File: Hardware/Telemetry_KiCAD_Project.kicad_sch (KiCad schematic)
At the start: 3 parts, among them J1 TX SPI Debug, J2 RX SPI Debug, J3 Right Angle SMA Female

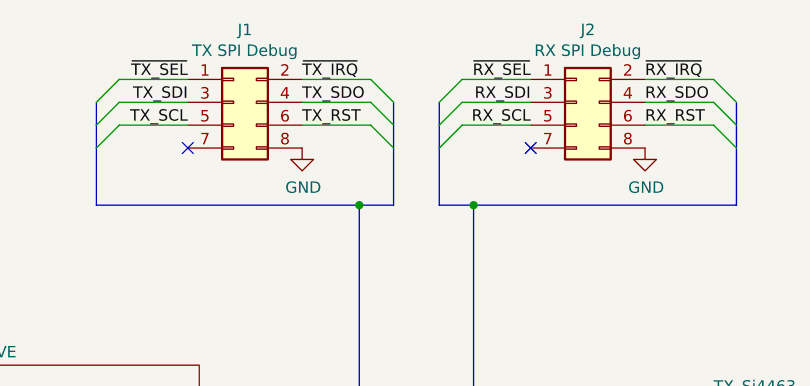
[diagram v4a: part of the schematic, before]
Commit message: Updated LCSC numbers, updated BOM file, added power LED.
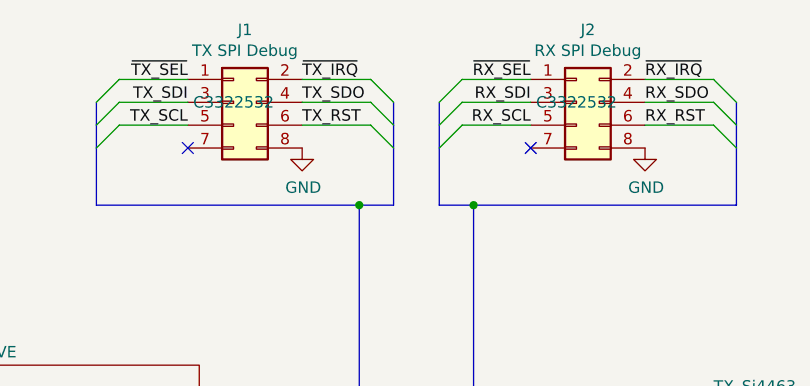
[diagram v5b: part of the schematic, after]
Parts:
- J1, J2: LCSC (none) -> C3322532
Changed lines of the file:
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@@
     (pin "1")
   )
-  (symbol (lib_id "Connector_Generic:Conn_02x04_Odd_Even") (at 107.95 24.13 0) (unit 1)
+  (symbol (lib_name "Conn_02x04_Odd_Even_1") (lib_id "Connector_Generic:Conn_02x04_Odd_Even") (at 107.95 24.13 0) (unit 1)
     (in_bom yes) (on_board yes)
     (property "Reference" "J1" (id 0) (at 109.22 16.0782 0))
@@
       (effects (font (size 1.27 1.27)) hide)
     )
+    (property "LCSC" "C3322532" (id 4) (at 107.95 24.13 0))
     (pin "1")
     (pin "2")
@@
       (effects (font (size 1.27 1.27)) hide)
     )
+    (property "LCSC" "C3322532" (id 4) (at 146.05 24.13 0))
     (pin "1")
     (pin "2")
@@
       (reference "#PWR047") (unit 1) (value "GND") (footprint "")
     )
+    (path "/00000000-0000-0000-0000-000061a107a5/7d5f7f73-c3ff-4d60-be90-7f89fb3f0e55"
+      (reference "#PWR048") (unit 1) (value "+3.3V") (footprint "")
+    )
+    (path "/00000000-0000-0000-0000-000061a107a5/32b6add9-6af3-4c4e-9640-6b64439e3a2a"
+      (reference "#PWR049") (unit 1) (value "GND") (footprint "")
+    )
     (path "/00000000-0000-0000-0000-000061a107a5/00000000-0000-0000-0000-000061a17dd9"
       (reference "#PWR050") (unit 1) (value "+3.3V") (footprint "")
@@
       (reference "D6") (unit 1) (value "Red") (footprint "LED_SMD:LED_0603_1608Metric_Pad1.05x0.95mm_HandSolder")
     )
+    (path "/00000000-0000-0000-0000-000061a107a5/8c687336-efb8-48b9-ac29-6b1477aa311d"
+      (reference "D7") (unit 1) (value "Red") (footprint "LED_SMD:LED_0603_1608Metric_Pad1.05x0.95mm_HandSolder")
+    )
     (path "/00000000-0000-0000-0000-000061a2ed84/00000000-0000-0000-0000-000061a399bc"
       (reference "FB1") (unit 1) (value "Ferrite_Bead_Small") (footprint "Capacitor_SMD:C_0603_1608Metric_Pad1.08x0.95mm_HandSolder")
@@
       (reference "R12") (unit 1) (value "4.7k") (footprint "Resistor_SMD:R_0603_1608Metric_Pad0.98x0.95mm_HandSolder")
     )
+    (path "/00000000-0000-0000-0000-000061a107a5/75ba48bc-fbe0-4662-9c97-6ba22e911647"
+      (reference "R13") (unit 1) (value "820") (footprint "Resistor_SMD:R_0603_1608Metric")
+    )
     (path "/00000000-0000-0000-0000-000061a107a5/00000000-0000-0000-0000-000061f1a897"

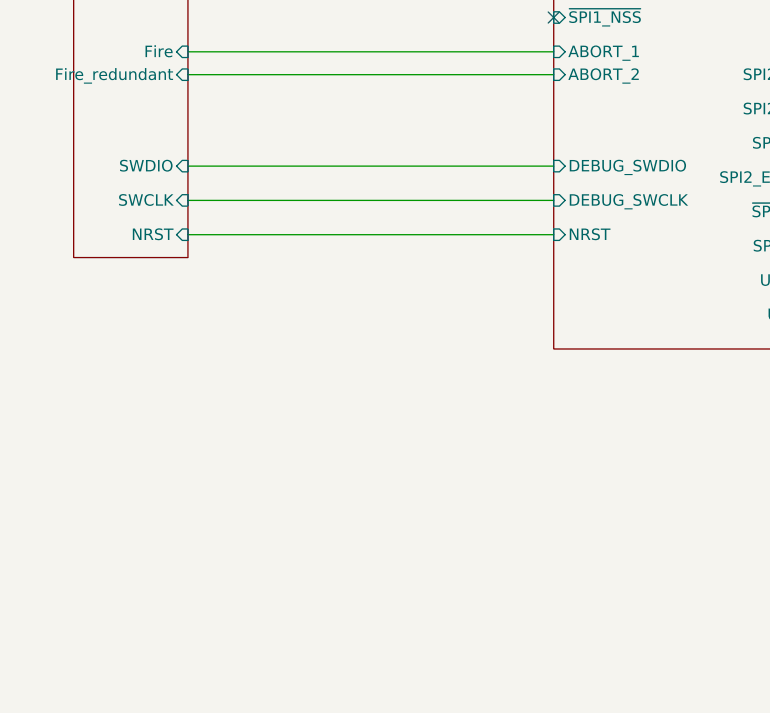
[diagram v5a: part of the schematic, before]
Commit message: Updated SPI pins. Added onboard JTAG header
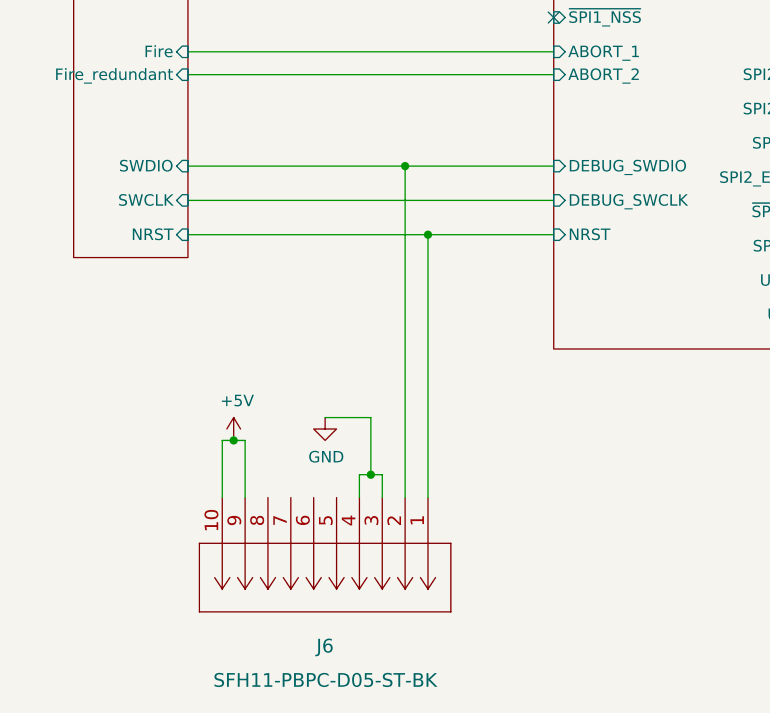
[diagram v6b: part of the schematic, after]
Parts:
- added J6: SFH11-PBPC-D05-ST-BK, jtag:SFH11-PBPC-D05-ST-BK, symbol JTAG:SFH11-PBPC-D05-ST-BK
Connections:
- net 37 Pin DSUB/NRST: now also J6.1
- net 37 Pin DSUB/SWDIO: now also J6.2
- net GND: now also J6.3, J6.4
- new net +5V: J6.10, J6.9
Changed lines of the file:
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@@
   (junction (at 134.62 35.56) (diameter 0) (color 0 0 0 0)
   )
+  (junction (at 52.07 134.62) (diameter 0) (color 0 0 0 0)
+  )
+  (junction (at 36.83 130.81) (diameter 0) (color 0 0 0 0)
+  )
+  (junction (at 55.88 100.33) (diameter 0) (color 0 0 0 0)
+  )
   (junction (at 121.92 57.15) (diameter 0) (color 0 0 0 0)
+  )
+  (junction (at 58.42 107.95) (diameter 0) (color 0 0 0 0)
   )
   (junction (at 134.62 87.63) (diameter 0) (color 0 0 0 0)
@@
     (stroke (width 0) (type default) (color 0 0 0 0))
   )
+  (wire (pts (xy 46.99 128.27) (xy 52.07 128.27))
+    (stroke (width 0) (type default) (color 0 0 0 0))
+  )
+  (wire (pts (xy 53.34 134.62) (xy 53.34 137.16))
+    (stroke (width 0) (type default) (color 0 0 0 0))
+  )
   (wire (pts (xy 104.14 113.03) (xy 125.73 113.03))
     (stroke (width 0) (type default) (color 0 0 0 0))
@@
     (stroke (width 0) (type default) (color 0 0 0 0))
   )
+  (wire (pts (xy 50.8 134.62) (xy 50.8 137.16))
+    (stroke (width 0) (type default) (color 0 0 0 0))
+  )
   (bus (pts (xy 134.62 35.56) (xy 130.81 35.56))
     (stroke (width 0) (type default) (color 0 0 0 0))
@@
     (stroke (width 0) (type default) (color 0 0 0 0))
   )
-  (wire (pts (xy 72.39 100.33) (xy 31.75 100.33))
+  (wire (pts (xy 72.39 100.33) (xy 55.88 100.33))
     (stroke (width 0) (type default) (color 0 0 0 0))
   )
@@
     (stroke (width 0) (type default) (color 0 0 0 0))
   )
-  (wire (pts (xy 72.39 107.95) (xy 31.75 107.95))
+  (wire (pts (xy 72.39 107.95) (xy 58.42 107.95))
     (stroke (width 0) (type default) (color 0 0 0 0))
   )
@@
     (stroke (width 0) (type default) (color 0 0 0 0))
   )
+  (wire (pts (xy 50.8 134.62) (xy 52.07 134.62))
+    (stroke (width 0) (type default) (color 0 0 0 0))
+  )
   (bus (pts (xy 130.81 24.13) (xy 130.81 26.67))
     (stroke (width 0) (type default) (color 0 0 0 0))
   )
+  (wire (pts (xy 35.56 130.81) (xy 35.56 137.16))
+    (stroke (width 0) (type default) (color 0 0 0 0))
+  )
   (wire (pts (xy 104.14 105.41) (xy 113.03 105.41))
     (stroke (width 0) (type default) (color 0 0 0 0))
   )
+  (wire (pts (xy 55.88 100.33) (xy 55.88 137.16))
+    (stroke (width 0) (type default) (color 0 0 0 0))
+  )
   (wire (pts (xy 113.03 68.58) (xy 104.14 68.58))
     (stroke (width 0) (type default) (color 0 0 0 0))
@@
     (stroke (width 0) (type default) (color 0 0 0 0))
   )
+  (wire (pts (xy 38.1 130.81) (xy 36.83 130.81))
+    (stroke (width 0) (type default) (color 0 0 0 0))
+  )
   (bus (pts (xy 121.92 57.15) (xy 140.97 57.15))
     (stroke (width 0) (type default) (color 0 0 0 0))
   )
+  (wire (pts (xy 58.42 107.95) (xy 31.75 107.95))
+    (stroke (width 0) (type default) (color 0 0 0 0))
+  )
   (bus (pts (xy 125.73 24.13) (xy 125.73 26.67))
     (stroke (width 0) (type default) (color 0 0 0 0))
@@
     (stroke (width 0) (type default) (color 0 0 0 0))
   )
+  (wire (pts (xy 52.07 128.27) (xy 52.07 134.62))
+    (stroke (width 0) (type default) (color 0 0 0 0))
+  )
   (bus (pts (xy 115.57 87.63) (xy 115.57 91.44))
     (stroke (width 0) (type default) (color 0 0 0 0))
@@
     (stroke (width 0) (type default) (color 0 0 0 0))
   )
+  (wire (pts (xy 55.88 100.33) (xy 31.75 100.33))
+    (stroke (width 0) (type default) (color 0 0 0 0))
+  )
   (wire (pts (xy 143.51 100.33) (xy 161.29 100.33))
     (stroke (width 0) (type default) (color 0 0 0 0))
@@
     (stroke (width 0) (type default) (color 0 0 0 0))
   )
+  (wire (pts (xy 38.1 137.16) (xy 38.1 130.81))
+    (stroke (width 0) (type default) (color 0 0 0 0))
+  )
   (bus (pts (xy 140.97 105.41) (xy 140.97 109.22))
     (stroke (width 0) (type default) (color 0 0 0 0))
@@
     (stroke (width 0) (type default) (color 0 0 0 0))
   )
+  (wire (pts (xy 36.83 130.81) (xy 35.56 130.81))
+    (stroke (width 0) (type default) (color 0 0 0 0))
+  )
   (bus (pts (xy 163.83 26.67) (xy 163.83 29.21))
     (stroke (width 0) (type default) (color 0 0 0 0))
   )
+  (wire (pts (xy 58.42 107.95) (xy 58.42 137.16))
+    (stroke (width 0) (type default) (color 0 0 0 0))
+  )
   (bus (pts (xy 140.97 68.58) (xy 140.97 72.39))
     (stroke (width 0) (type default) (color 0 0 0 0))
@@
   )
   (wire (pts (xy 153.67 133.35) (xy 120.65 133.35))
+    (stroke (width 0) (type default) (color 0 0 0 0))
+  )
+  (wire (pts (xy 52.07 134.62) (xy 53.34 134.62))
     (stroke (width 0) (type default) (color 0 0 0 0))
   )
@@
     (pin "1")
   )
+  (symbol (lib_id "power:GND") (at 46.99 128.27 0) (unit 1)
+    (in_bom yes) (on_board yes)
+    (property "Reference" "#PWR?" (id 0) (at 46.99 134.62 0)
+      (effects (font (size 1.27 1.27)) hide)
+    )
+    (property "Value" "GND" (id 1) (at 47.117 132.6642 0))
+    (property "Footprint" "" (id 2) (at 46.99 128.27 0)
+      (effects (font (size 1.27 1.27)) hide)
+    )
+    (property "Datasheet" "" (id 3) (at 46.99 128.27 0)
+      (effects (font (size 1.27 1.27)) hide)
+    )
+    (pin "1")
+  )
+  (symbol (lib_id "JTAG:SFH11-PBPC-D05-ST-BK") (at 58.42 137.16 270) (unit 1)
+    (in_bom yes) (on_board yes) (fields_autoplaced)
+    (property "Reference" "J6" (id 0) (at 46.99 153.67 90)
+      (effects (font (size 1.524 1.524)))
+    )
+    (property "Value" "SFH11-PBPC-D05-ST-BK" (id 1) (at 46.99 157.48 90)
+      (effects (font (size 1.524 1.524)))
+    )
+    (property "Footprint" "jtag:SFH11-PBPC-D05-ST-BK" (id 2) (at 46.736 147.32 0)
+      (effects (font (size 1.524 1.524)) hide)
+    )
+    (property "Datasheet" "https://s3.amazonaws.com/catalogspreads-pdf/PAGE123%20.100%20SFH11%20SERIES%20FEMALE%20HDR%20ST%20RA.pdf" (id 3) (at 58.42 137.16 0)
+      (effects (font (size 1.524 1.524)) hide)
+    )
+    (pin "1")
+    (pin "10")
+    (pin "2")
+    (pin "3")
+    (pin "4")
+    (pin "5")
+    (pin "6")
+    (pin "7")
+    (pin "8")
+    (pin "9")
+  )
+  (symbol (lib_id "power:+5V") (at 36.83 130.81 0) (unit 1)
+    (in_bom yes) (on_board yes)
+    (property "Reference" "#PWR?" (id 0) (at 36.83 134.62 0)
+      (effects (font (size 1.27 1.27)) hide)
+    )
+    (property "Value" "+5V" (id 1) (at 37.211 126.4158 0))
+    (property "Footprint" "" (id 2) (at 36.83 130.81 0)
+      (effects (font (size 1.27 1.27)) hide)
+    )
+    (property "Datasheet" "" (id 3) (at 36.83 130.81 0)
+      (effects (font (size 1.27 1.27)) hide)
+    )
+    (pin "1")
+  )
   (sheet (at 161.29 57.15) (size 17.78 24.13) (fields_autoplaced)
     (stroke (width 0) (type solid) (color 0 0 0 0))
@@
       (reference "#PWR0132") (unit 1) (value "+3.3V") (footprint "")
     )
+    (path "/212966e5-f820-477b-86df-bae7c75f8aac"
+      (reference "#PWR?") (unit 1) (value "GND") (footprint "")
+    )
+    (path "/6441d917-d612-4f49-8582-fdcec76e8233"
+      (reference "#PWR?") (unit 1) (value "+5V") (footprint "")
+    )
     (path "/00000000-0000-0000-0000-000061a0416a/00000000-0000-0000-0000-0000619f8bd8"
       (reference "C1") (unit 1) (value "100pF") (footprint "Capacitor_SMD:C_0402_1005Metric")
@@
       (reference "J5") (unit 1) (value "DB37_Male_MountingHoles") (footprint "RDT_Custom_Footprints:L717SDC37P1ACH4F")
     )
+    (path "/2b0e9e96-51da-4bec-9e9d-854cf7509a54"
+      (reference "J6") (unit 1) (value "SFH11-PBPC-D05-ST-BK") (footprint "jtag:SFH11-PBPC-D05-ST-BK")
+    )
     (path "/00000000-0000-0000-0000-000061a107a5/00000000-0000-0000-0000-000061f76154"

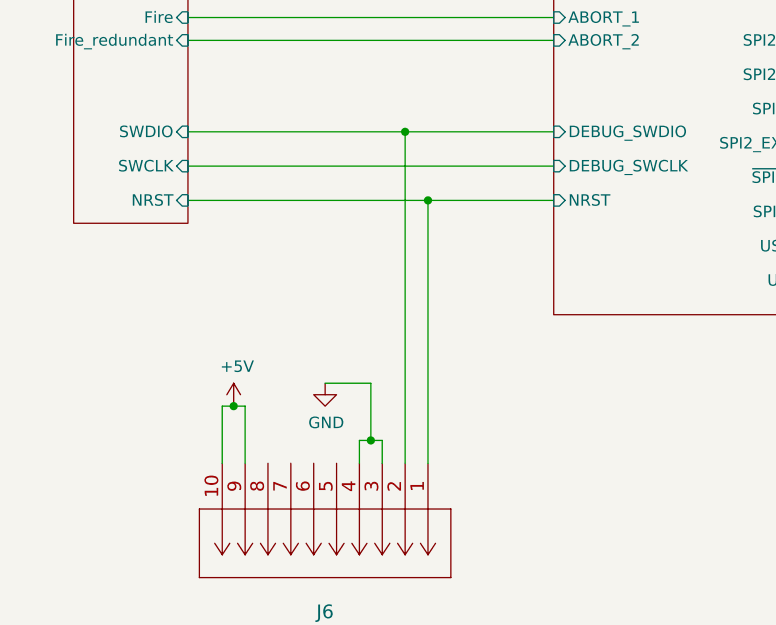
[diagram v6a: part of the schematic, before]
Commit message: Routed JTAG connector and set boot0 default to GND
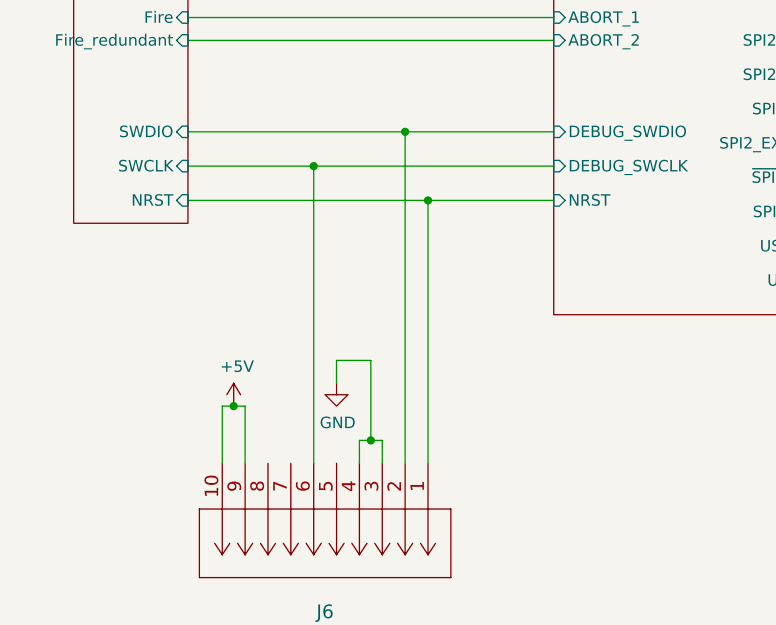
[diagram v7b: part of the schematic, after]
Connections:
- net 37 Pin DSUB/SWCLK: now also J6.6
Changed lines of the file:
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@@
   (junction (at 55.88 100.33) (diameter 0) (color 0 0 0 0)
+  )
+  (junction (at 45.72 104.14) (diameter 0) (color 0 0 0 0)
   )
   (junction (at 121.92 57.15) (diameter 0) (color 0 0 0 0)
@@
     (stroke (width 0) (type default) (color 0 0 0 0))
   )
-  (wire (pts (xy 46.99 128.27) (xy 52.07 128.27))
+  (wire (pts (xy 48.26 125.73) (xy 52.07 125.73))
     (stroke (width 0) (type default) (color 0 0 0 0))
   )
@@
     (stroke (width 0) (type default) (color 0 0 0 0))
   )
+  (wire (pts (xy 48.26 125.73) (xy 48.26 128.27))
+    (stroke (width 0) (type default) (color 0 0 0 0))
+  )
   (bus (pts (xy 115.57 99.06) (xy 115.57 102.87))
     (stroke (width 0) (type default) (color 0 0 0 0))
@@
     (stroke (width 0) (type default) (color 0 0 0 0))
   )
-  (wire (pts (xy 52.07 128.27) (xy 52.07 134.62))
+  (wire (pts (xy 52.07 125.73) (xy 52.07 134.62))
     (stroke (width 0) (type default) (color 0 0 0 0))
   )
@@
     (stroke (width 0) (type default) (color 0 0 0 0))
   )
+  (wire (pts (xy 45.72 104.14) (xy 45.72 137.16))
+    (stroke (width 0) (type default) (color 0 0 0 0))
+  )
   (bus (pts (xy 115.57 91.44) (xy 115.57 95.25))
     (stroke (width 0) (type default) (color 0 0 0 0))
@@
     (stroke (width 0) (type default) (color 0 0 0 0))
   )
-  (wire (pts (xy 31.75 104.14) (xy 72.39 104.14))
+  (wire (pts (xy 31.75 104.14) (xy 45.72 104.14))
     (stroke (width 0) (type default) (color 0 0 0 0))
   )
@@
   )
   (bus (pts (xy 140.97 101.6) (xy 140.97 105.41))
+    (stroke (width 0) (type default) (color 0 0 0 0))
+  )
+  (wire (pts (xy 45.72 104.14) (xy 72.39 104.14))
     (stroke (width 0) (type default) (color 0 0 0 0))
   )
@@
     (pin "1")
   )
-  (symbol (lib_id "power:GND") (at 46.99 128.27 0) (unit 1)
+  (symbol (lib_id "power:GND") (at 48.26 128.27 0) (unit 1)
     (in_bom yes) (on_board yes)
-    (property "Reference" "#PWR?" (id 0) (at 46.99 134.62 0)
-      (effects (font (size 1.27 1.27)) hide)
-    )
-    (property "Value" "GND" (id 1) (at 47.117 132.6642 0))
-    (property "Footprint" "" (id 2) (at 46.99 128.27 0)
-      (effects (font (size 1.27 1.27)) hide)
-    )
-    (property "Datasheet" "" (id 3) (at 46.99 128.27 0)
+    (property "Reference" "#PWR0133" (id 0) (at 48.26 134.62 0)
+      (effects (font (size 1.27 1.27)) hide)
+    )
+    (property "Value" "GND" (id 1) (at 48.387 132.6642 0))
+    (property "Footprint" "" (id 2) (at 48.26 128.27 0)
+      (effects (font (size 1.27 1.27)) hide)
+    )
+    (property "Datasheet" "" (id 3) (at 48.26 128.27 0)
       (effects (font (size 1.27 1.27)) hide)
     )
@@
   (symbol (lib_id "power:+5V") (at 36.83 130.81 0) (unit 1)
     (in_bom yes) (on_board yes)
-    (property "Reference" "#PWR?" (id 0) (at 36.83 134.62 0)
+    (property "Reference" "#PWR0134" (id 0) (at 36.83 134.62 0)
       (effects (font (size 1.27 1.27)) hide)
     )
@@
     )
     (path "/212966e5-f820-477b-86df-bae7c75f8aac"
-      (reference "#PWR?") (unit 1) (value "GND") (footprint "")
+      (reference "#PWR0133") (unit 1) (value "GND") (footprint "")
     )
     (path "/6441d917-d612-4f49-8582-fdcec76e8233"
-      (reference "#PWR?") (unit 1) (value "+5V") (footprint "")
+      (reference "#PWR0134") (unit 1) (value "+5V") (footprint "")
     )
     (path "/00000000-0000-0000-0000-000061a0416a/00000000-0000-0000-0000-0000619f8bd8"

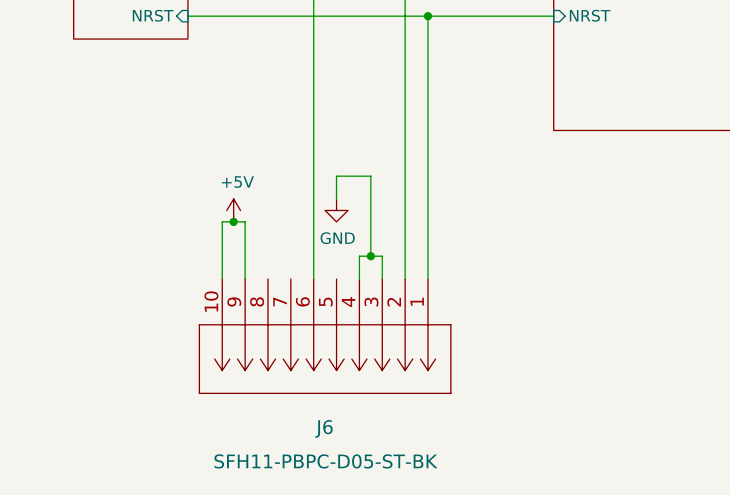
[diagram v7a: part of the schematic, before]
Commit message: Added LCSC Number to JTAG connector
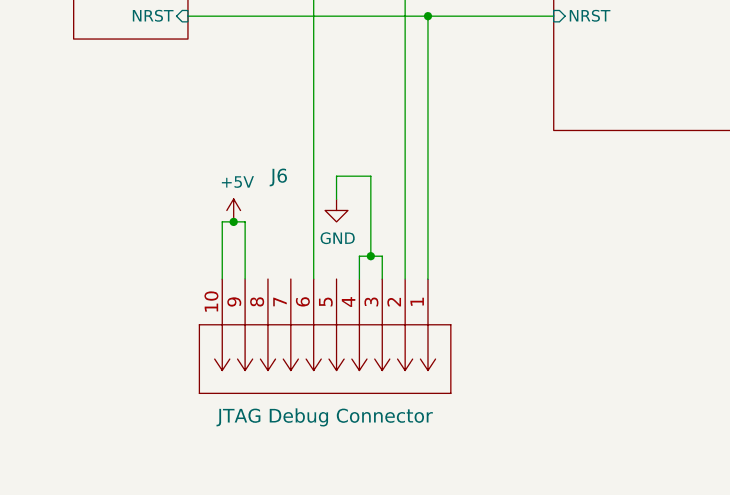
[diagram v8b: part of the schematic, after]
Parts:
- J6: value SFH11-PBPC-D05-ST-BK -> JTAG Debug Connector; LCSC (none) -> C3322462
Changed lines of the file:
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@@
   )
   (symbol (lib_id "JTAG:SFH11-PBPC-D05-ST-BK") (at 58.42 137.16 270) (unit 1)
-    (in_bom yes) (on_board yes) (fields_autoplaced)
-    (property "Reference" "J6" (id 0) (at 46.99 153.67 90)
+    (in_bom yes) (on_board yes)
+    (property "Reference" "J6" (id 0) (at 41.91 125.73 90)
       (effects (font (size 1.524 1.524)))
     )
-    (property "Value" "SFH11-PBPC-D05-ST-BK" (id 1) (at 46.99 157.48 90)
+    (property "Value" "JTAG Debug Connector" (id 1) (at 46.99 152.4 90)
       (effects (font (size 1.524 1.524)))
     )
-    (property "Footprint" "jtag:SFH11-PBPC-D05-ST-BK" (id 2) (at 46.736 147.32 0)
+    (property "Footprint" "jtag:SFH11-PBPC-D05-ST-BK" (id 2) (at 48.26 125.476 0)
       (effects (font (size 1.524 1.524)) hide)
     )
     (property "Datasheet" "https://s3.amazonaws.com/catalogspreads-pdf/PAGE123%20.100%20SFH11%20SERIES%20FEMALE%20HDR%20ST%20RA.pdf" (id 3) (at 58.42 137.16 0)
       (effects (font (size 1.524 1.524)) hide)
+    )
+    (property "LCSC" "C3322462" (id 4) (at 58.42 137.16 0)
+      (effects (font (size 1.27 1.27)) hide)
     )
     (pin "1")
@@
     )
     (path "/2b0e9e96-51da-4bec-9e9d-854cf7509a54"
-      (reference "J6") (unit 1) (value "SFH11-PBPC-D05-ST-BK") (footprint "jtag:SFH11-PBPC-D05-ST-BK")
+      (reference "J6") (unit 1) (value "JTAG Debug Connector") (footprint "jtag:SFH11-PBPC-D05-ST-BK")
     )
     (path "/00000000-0000-0000-0000-000061a107a5/00000000-0000-0000-0000-000061f76154"
